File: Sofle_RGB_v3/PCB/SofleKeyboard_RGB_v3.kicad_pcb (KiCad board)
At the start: 2 copper layers, 142.1 x 111.8 mm, 100 parts, among them J1 LED, J2 4PIN, J3 OLED, J4 key leds, J5 backlight sel, J6 indicator bypass, J7 BAT, P1 i2c_pin, P2 i2c_pin, SW1 SW_PUSH-MX_W_LED, SW10 SW_PUSH-MX_W_LED, SW11 SW_PUSH-MX_W_LED, SW12 SW_PUSH-MX_W_LED, SW13 SW_PUSH-MX_W_LED, SW14 SW_PUSH-MX_W_LED, SW15 SW_PUSH-MX_W_LED, SW16 SW_PUSH-MX_W_LED, SW17 SW_PUSH-MX_W_LED, SW18 SW_PUSH-MX_W_LED, SW19 SW_PUSH-MX_W_LED, SW2 SW_PUSH-MX_W_LED, SW20 SW_PUSH-MX_W_LED, SW21 SW_PUSH-MX_W_LED, SW22 SW_PUSH-MX_W_LED, SW23 SW_PUSH-MX_W_LED, SW24 SW_PUSH-MX_W_LED, SW25 Rotary_Encoder_Switch, SW26 SW_PUSH-MX_W_LED, SW27 SW_PUSH-MX_W_LED, SW28 SW_PUSH-MX_W_LED, SW29 SW_PUSH-MX_W_LED, SW3 SW_PUSH-MX_W_LED, SW30 SW_PUSH-MX_W_LED, SW31 PWR Top, SW32 PWR Bottom, SW4 SW_PUSH-MX_W_LED, SW5 SW_PUSH-MX_W_LED, SW6 SW_PUSH-MX_W_LED, SW7 SW_PUSH-MX_W_LED, SW8 SW_PUSH-MX_W_LED, SW9 SW_PUSH-MX_W_LED, U1 ProMicro

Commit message: Sofle RGB V3.2 with native nice!view support
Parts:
- removed J4: key leds, Connector:3x1header
- removed J5: backlight sel, Connector:3x1header
- removed J6: indicator bypass, Connector:3x1header
- removed P1, P2: i2c_pin, SofleKeyboard-footprint:1pin_conn
- removed R1, R2: R, SofleKeyboard-footprint:RESISTOR_mini
- removed W1: Jumper, Jumper:SolderJumper-2_P1.3mm_Bridged_RoundedPad1.0x1.5mm
- added J8: nice!view, SofleKeyboard-footprint:niceview_5Pin, F.Cu at (95.4, 75.9)
- added J9: B-, SofleKeyboard-footprint:1pin_conn, F.Cu at (107.5, 72.7)
- added JP10: Jumper_NO_Small, SofleKeyboard-footprint:Jumper, F.Cu at (103.0, 78.6)
- added JP11: Jumper_NO_Small, SofleKeyboard-footprint:Jumper, F.Cu at (98.0, 78.6)
- added JP12: Jumper_NO_Small, SofleKeyboard-footprint:Jumper, F.Cu at (95.4, 78.6)
- added JP13: Jumper_NO_Small, SofleKeyboard-footprint:Jumper, B.Cu at (105.6, 78.6)
- added JP14: Jumper_NO_Small, SofleKeyboard-footprint:Jumper, B.Cu at (103.0, 78.6)
- added JP15: Jumper_NO_Small, SofleKeyboard-footprint:Jumper, B.Cu at (98.0, 78.6)
- added JP16: Jumper_NO_Small, SofleKeyboard-footprint:Jumper, B.Cu at (95.4, 78.6)
- added JP18: Indicator Bypass, Jumper:SolderJumper-2_P1.3mm_Open_TrianglePad1.0x1.5mm, F.Cu at (112.2, 83.2)
- added JP19: Underglow Bypass, Jumper:SolderJumper-2_P1.3mm_Open_TrianglePad1.0x1.5mm, F.Cu at (185.0, 101.8)
- added JP9: Jumper_NO_Small, SofleKeyboard-footprint:Jumper, F.Cu at (105.6, 78.6)
- D1, D10, D11, D12, D14, D15, D16, D17, D18, D19, D2, D20, D21, D22, D23, D24, D25, D26, D27, D28, D29, D3, D30, D4, D5, D6, D7, D8, D9: footprint Diode_SMD:crkbd-diode -> SofleKeyboard-footprint:SOD-223_with_cutout
- D13: footprint Diode_SMD:crkbd-diode -> SofleKeyboard-footprint:SOD-223_with_cutout; moved to B.Cu
- D31, D32, D33, D34, D35, D36, D37: footprint LED_SMD:SK6812MINI_underglow_dev -> SofleKeyboard-footprint:SK6812MINI_underglow_with_cutout
- J2: footprint SofleKeyboard-footprint:MJ-4PP-9 -> SofleKeyboard-footprint:PJ-320A_double_sided_with_cutouts
- J7: value BAT -> B+; footprint Connector_PinHeader_2.54mm:PinHeader_1x02_P2.54mm_Vertical -> SofleKeyboard-footprint:1pin_conn
- SW1, SW10, SW11, SW12, SW13, SW14, SW15, SW16, SW17, SW18, SW19, SW2, SW20, SW21, SW22, SW23, SW24, SW26, SW27, SW28, SW29, SW3, SW30, SW4, SW5, SW6, SW7, SW8, SW9: footprint Button_Switch_Keyboard:SK6812MINI_and_cherry -> SofleKeyboard-footprint:SK6812MINI_and_cherry_with_cutouts
- SW25: footprint SofleKeyboard-footprint:RotaryEncoder_Alps_EC11E-Switch_Vertical_H20mm-keebio_modified -> SofleKeyboard-footprint:RotaryEncoder_Alps_EC11E-Switch_Vertical_H20mm-keebio_modified_with_cutouts
- U1: footprint SofleKeyboard-footprint:ProMicro -> SofleKeyboard-footprint:ProMicro_with_cutouts
- moved G*** 96.9 mm to (94.8, 119.0)
- moved G*** 96.9 mm to (94.0, 119.0)
- moved J7 33.1 mm to (93.5, 72.7), turned to 0 degrees
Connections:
- D33 pad 3: /underglow -> underglow
- D36 pad 1: Net-(D36-Pad1) -> unconnected-(D36-DOUT-Pad1)_0
- D37 pad 1: lights -> underglow
- D37 pad 3: Net-(D37-Pad3) -> RGB
- J1 pad 2: LED -> RGB
- J2 pad 3: /i2c_d -> DATA
- J2 pad 4: /i2c_c -> unconnected-(J2-Pad4)
- SW24 pad 3: Net-(SW24-Pad3) -> col1
- SW30 pad 1: Net-(SW24-Pad3) -> col1
- SW30 pad 3: /backlight -> backlight
- SW31 pad 1: unconnected-(SW31-Pad1) -> RAW
- SW31 pad 3: RAW -> unconnected-(SW31-C-Pad3)
- SW32 pad 1: RAW -> unconnected-(SW32-A-Pad1)
- SW32 pad 3: unconnected-(SW32-Pad3) -> RAW
- U1 pad 1: LED -> CS
- U1 pad 7: unconnected-(U1-Pad7) -> RGB
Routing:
- net underglow: track 0.00 -> 148.7 mm, vias 0 -> 9
- net lights: track 118.6 -> 0.00 mm, vias 5 -> 0
- net CS: track 0.00 -> 72.6 mm, vias 0 -> 4
- net LED: track 67.7 -> 0.00 mm, vias 2 -> 0
- net RGB: track 0.00 -> 57.1 mm, vias 0 -> 4
- net col1: track 299.9 -> 346.6 mm, vias 15 -> 17
- net Net-(SW24-Pad3): track 46.6 -> 0.00 mm, vias 3 -> 0
- net /underglow: track 42.3 -> 0.00 mm, vias 3 -> 0
- net BAT: track 49.2 -> 12.4 mm
- net /backlight: track 27.0 -> 0.00 mm, vias 1 -> 0
- net /i2c_d: track 26.8 -> 0.00 mm
- net backlight: track 0.00 -> 24.8 mm, vias 0 -> 2
- net unconnected-(U1-Pad7): track 17.0 -> 0.00 mm, vias 1 -> 0
- net DATA: track 47.8 -> 64.2 mm
- net RESET: track 64.6 -> 76.9 mm
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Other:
- board text added: "Indicator Bypass"
- board text added: "OLED"
- board text added: "Sofle RGB by Dane Evans / v3.2 by 42. Keebs"
- board text added: "nice!view"
- board text removed: "&BL"
- board text removed: "BL"
- board text removed: "BYP"
- board text removed: "Backlight enable"
- board text removed: "ENA"
- board text removed: "IND"
- board text removed: "Ind bypass"
- board text removed: "Light Sel"
- board text removed: "Sofle RGB v3 by Dane Evans x piit79"
- board text removed: "Sofle RGB v3, Dane Evans x piit79"
- board text removed: "UND"

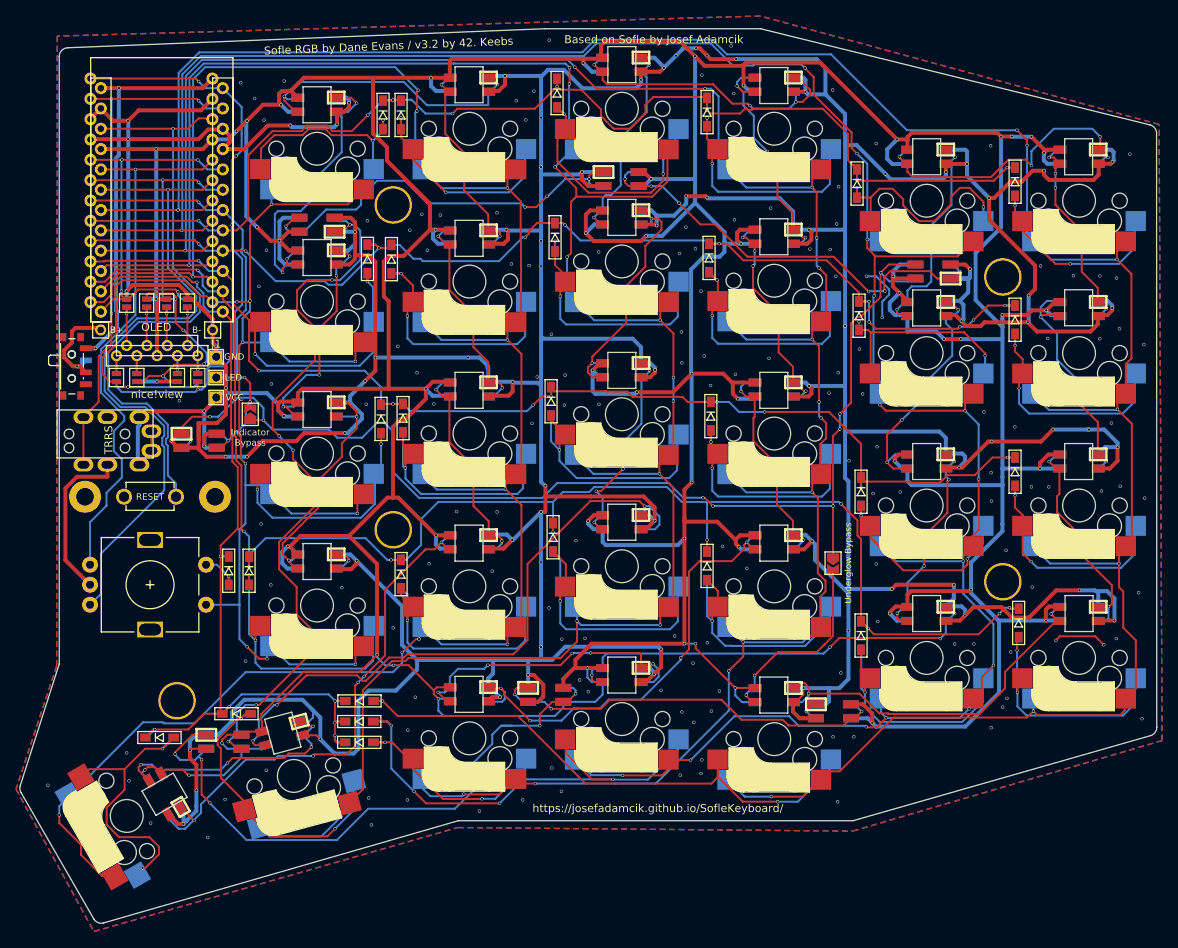
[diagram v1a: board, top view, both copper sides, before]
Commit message: Sofle RGB V3.4
* Fix missing connection between underglow and backlight
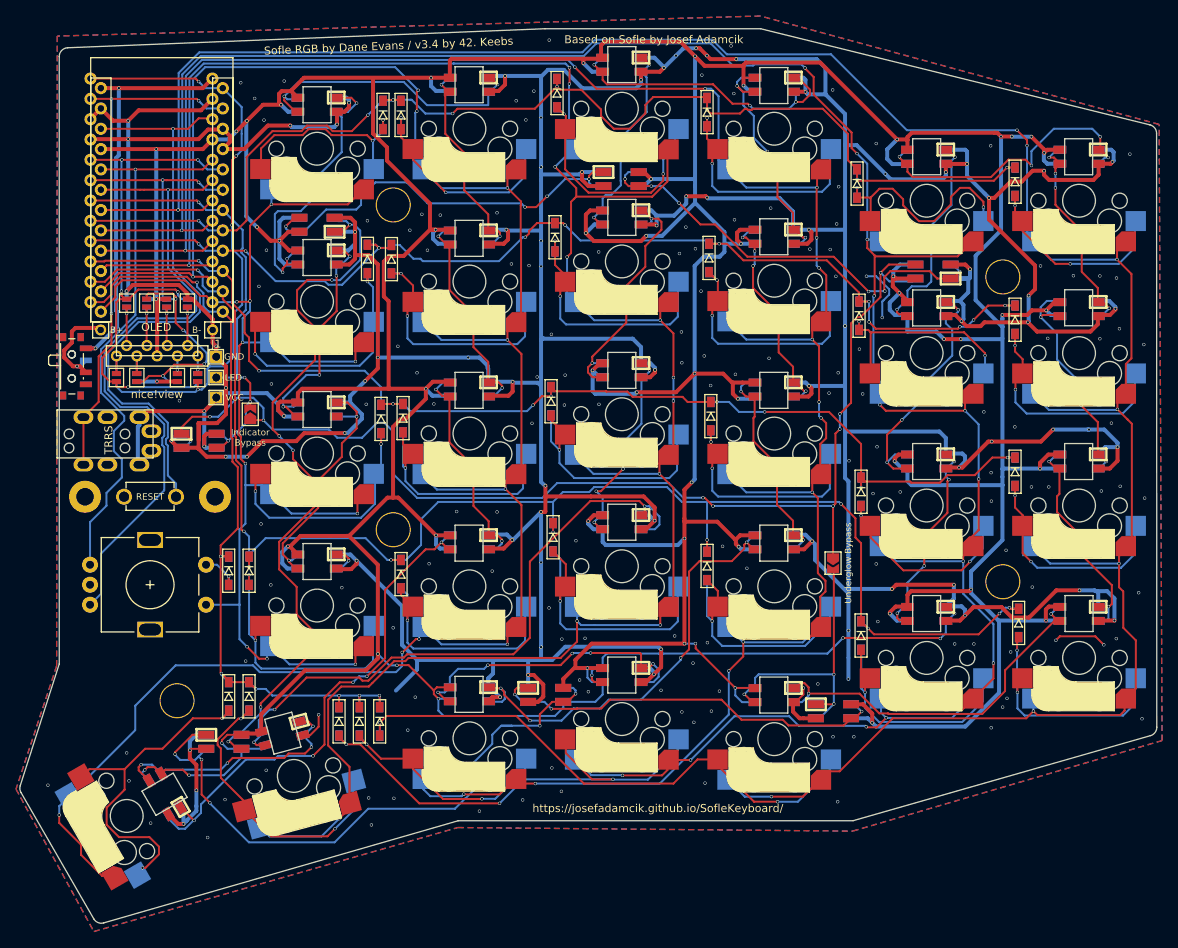
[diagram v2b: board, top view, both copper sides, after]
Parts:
- moved D26 10.1 mm to (109.5, 118.5), turned to -90 degrees
- moved D30 3.60 mm to (128.3, 121.6), turned to -90 degrees
- moved D27 2.69 mm to (112.0, 118.5), turned to -90 degrees
- moved D28 2.62 mm to (125.8, 121.6), turned to -90 degrees
- moved D29 2.53 mm to (123.2, 121.6), turned to -90 degrees
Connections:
- D36 pad 1: unconnected-(D36-DOUT-Pad1)_0 -> backlight
- SW24 pad 3: col1 -> Net-(SW24B-DIN)
- SW30 pad 1: col1 -> Net-(SW24B-DIN)
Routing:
- net GND: track 985.2 -> 915.6 mm, vias 225 -> 224
- net Net-(SW24B-DIN): track 0.00 -> 47.5 mm, vias 0 -> 2
- net col1: track 346.6 -> 299.5 mm, vias 17 -> 15
- net row4: track 118.2 -> 103.1 mm
- net backlight: track 24.8 -> 36.9 mm, vias 2 -> 3
- net Net-(D26-A): track 36.1 -> 43.8 mm
- net col3: track 274.7 -> 278.8 mm
- net unconnected-(D36-DOUT-Pad1): track 3.12 -> 0.00 mm, vias 1 -> 0
- net Net-(D28-A): track 26.9 -> 29.7 mm
- net col4: track 258.8 -> 261.4 mm
- net unconnected-(J2-Pad4): track 2.45 -> 0.00 mm
- net Net-(D31-DOUT): track 92.8 -> 91.3 mm
- net Net-(D30-A): track 71.2 -> 70.1 mm
- net Net-(SW20B-DIN): track 65.3 -> 64.6 mm
- net Net-(D12-A): track 29.6 -> 30.1 mm
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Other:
- rule pad_to_mask_clearance: 0.2 -> 0
- board text added: "Sofle RGB by Dane Evans / v3.4 by 42. Keebs"
- board text removed: "Sofle RGB by Dane Evans / v3.2 by 42. Keebs"
